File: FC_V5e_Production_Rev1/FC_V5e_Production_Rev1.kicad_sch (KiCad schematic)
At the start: 75 parts, among them IC3 RV-3028-C7_32.768kHz_1ppm_TA_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, J12 USB_C_Receptacle_USB2.0_16P, J16 DEBUG, J18 Payload, J22 SWD Port, J3 Life Makes Lemonade, J5 BM04B-SRSS-TB(LF)(SN), SW1 KMR2, SW2 KMR2, U13 E22-400M30S, U14 TCA4307DGKR, U15 LIS2MDL, U2 ZDSD04GLGEAG, U3 TCA9548APWR, U30 E28-2G4M27S, U7 LSM6DSOTR

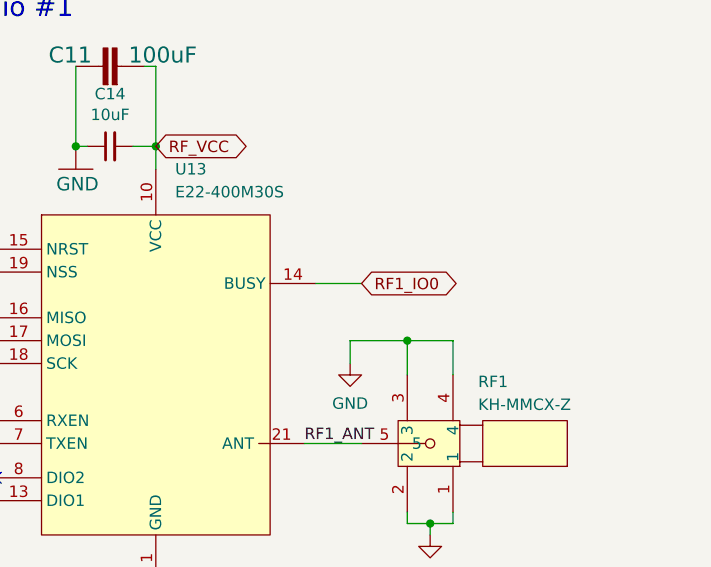
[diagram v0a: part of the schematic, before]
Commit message: V5e_Rev1: Added Pulldowns to RF1 IO
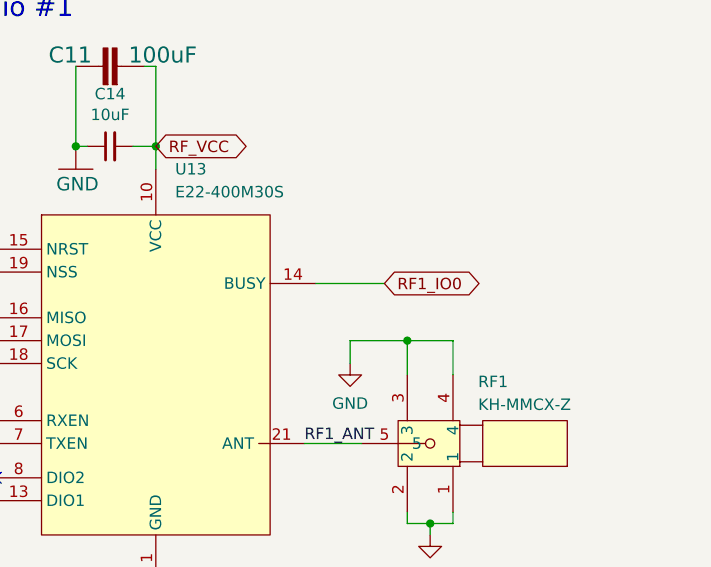
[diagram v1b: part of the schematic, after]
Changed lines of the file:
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@@
 	(wire
 		(pts
-			(xy 382.27 210.82) (xy 377.19 210.82)
+			(xy 384.81 210.82) (xy 377.19 210.82)
 		)
 		(stroke
@@
 	(global_label "RF1_IO0"
 		(shape bidirectional)
-		(at 382.27 210.82 0)
+		(at 384.81 210.82 0)
 		(fields_autoplaced yes)
 		(effects
@@
 		)
 		(property "Intersheetrefs" "${INTERSHEET_REFS}"
-			(at 394.047 210.82 0)
+			(at 396.587 210.82 0)
 			(hide yes)
 			(show_name no)

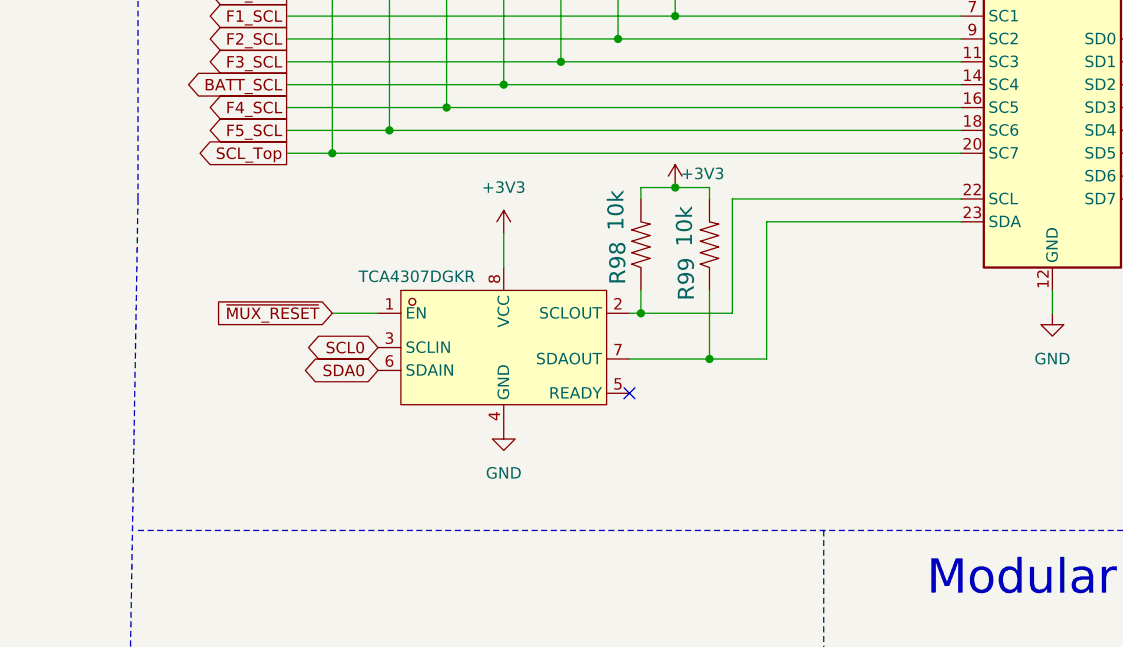
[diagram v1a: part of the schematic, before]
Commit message: V5e_Rev1: Removed TCA4307
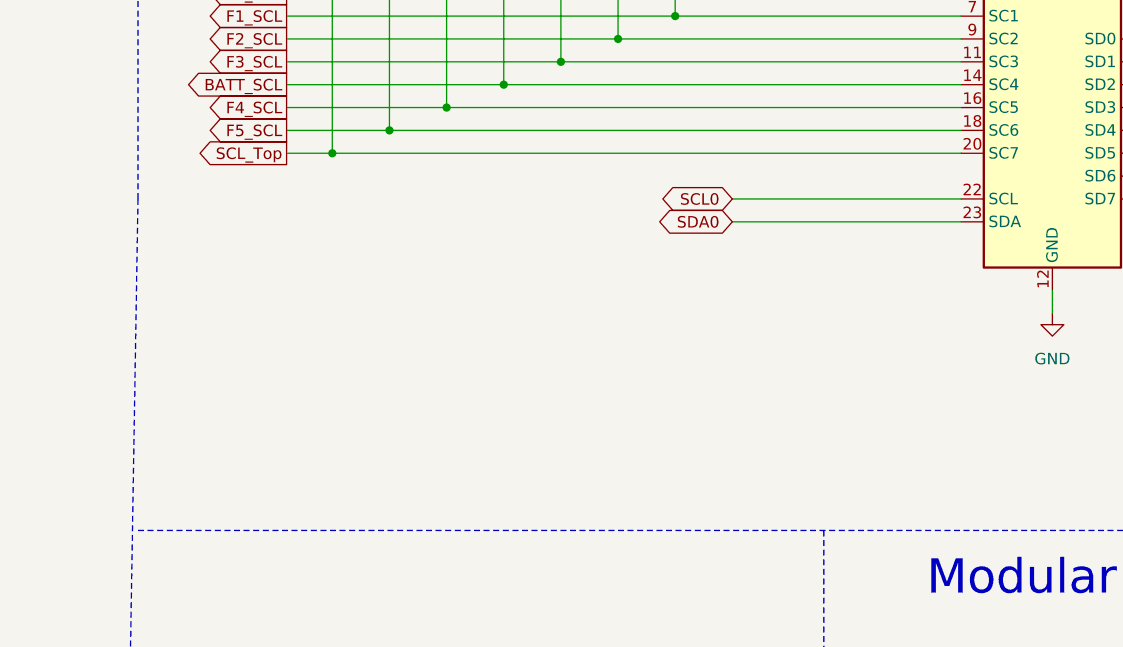
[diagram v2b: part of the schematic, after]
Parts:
- removed R98, R99: 10k, Resistor_SMD:R_0603_1608Metric, symbol mainboard:RESISTOR0603
- removed U14: TCA4307DGKR, easyeda2kicad:VSSOP-8_L3.0-W3.0-P0.65-LS4.9-BL, symbol easyeda2kicad:TCA4307DGKR
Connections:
- net SCL0: now also U3.22 (SCL)
- net SDA0: now also U3.23 (SDA)
- no-connect marks 14 -> 13

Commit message: V5e_Rev1: Rewired for Molex
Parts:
- R105, R106, R45, R57, R58, R59, R60, R61, R62, R72, R73, R88, R89: footprint Resistor_SMD:R_0603_1608Metric -> Resistor_SMD:R_0402_1005Metric
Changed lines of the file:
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@@
 			)
 		)
-		(property "Footprint" "Resistor_SMD:R_0603_1608Metric"
+		(property "Footprint" "Resistor_SMD:R_0402_1005Metric"
 			(at 345.44 109.22 0)
 			(hide yes)
@@
 			)
 		)
-		(property "Footprint" "Resistor_SMD:R_0603_1608Metric"
+		(property "Footprint" "Resistor_SMD:R_0402_1005Metric"
 			(at 351.79 109.22 0)
 			(hide yes)
@@
 			)
 		)
-		(property "Footprint" "Resistor_SMD:R_0603_1608Metric"
+		(property "Footprint" "Resistor_SMD:R_0402_1005Metric"
 			(at 368.3 109.22 0)
 			(hide yes)
@@
 			)
 		)
-		(property "Footprint" "Resistor_SMD:R_0603_1608Metric"
+		(property "Footprint" "Resistor_SMD:R_0402_1005Metric"
 			(at 374.65 109.22 0)
 			(hide yes)
@@
 			)
 		)
-		(property "Footprint" "Resistor_SMD:R_0603_1608Metric"
+		(property "Footprint" "Resistor_SMD:R_0402_1005Metric"
 			(at 257.81 104.14 0)
 			(hide yes)
@@
 			)
 		)
-		(property "Footprint" "Resistor_SMD:R_0603_1608Metric"
+		(property "Footprint" "Resistor_SMD:R_0402_1005Metric"
 			(at 238.76 104.14 0)
 			(hide yes)
@@
 			)
 		)
-		(property "Footprint" "Resistor_SMD:R_0603_1608Metric"
+		(property "Footprint" "Resistor_SMD:R_0402_1005Metric"
 			(at 361.95 107.95 0)
 			(hide yes)
@@
 			)
 		)
-		(property "Footprint" "Resistor_SMD:R_0603_1608Metric"
+		(property "Footprint" "Resistor_SMD:R_0402_1005Metric"
 			(at 387.35 109.22 0)
 			(hide yes)
@@
 			)
 		)
-		(property "Footprint" "Resistor_SMD:R_0603_1608Metric"
+		(property "Footprint" "Resistor_SMD:R_0402_1005Metric"
 			(at 381 109.22 0)
 			(hide yes)
@@
 			)
 		)
-		(property "Footprint" "Resistor_SMD:R_0603_1608Metric"
+		(property "Footprint" "Resistor_SMD:R_0402_1005Metric"
 			(at 276.86 104.14 0)
 			(hide yes)
@@
 			)
 		)
-		(property "Footprint" "Resistor_SMD:R_0603_1608Metric"
+		(property "Footprint" "Resistor_SMD:R_0402_1005Metric"
 			(at 251.46 104.14 0)
 			(hide yes)
@@
 			)
 		)
-		(property "Footprint" "Resistor_SMD:R_0603_1608Metric"
+		(property "Footprint" "Resistor_SMD:R_0402_1005Metric"
 			(at 245.11 104.14 0)
 			(hide yes)
@@
 			)
 		)
-		(property "Footprint" "Resistor_SMD:R_0603_1608Metric"
+		(property "Footprint" "Resistor_SMD:R_0402_1005Metric"
 			(at 356.87 109.22 0)
 			(hide yes)
